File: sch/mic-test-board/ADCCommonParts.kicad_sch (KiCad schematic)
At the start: 16 parts, among them U1 LMK1C1102, U3 MAX6070BAUT41+T, X1 KC3225Z32.7680C1KX00

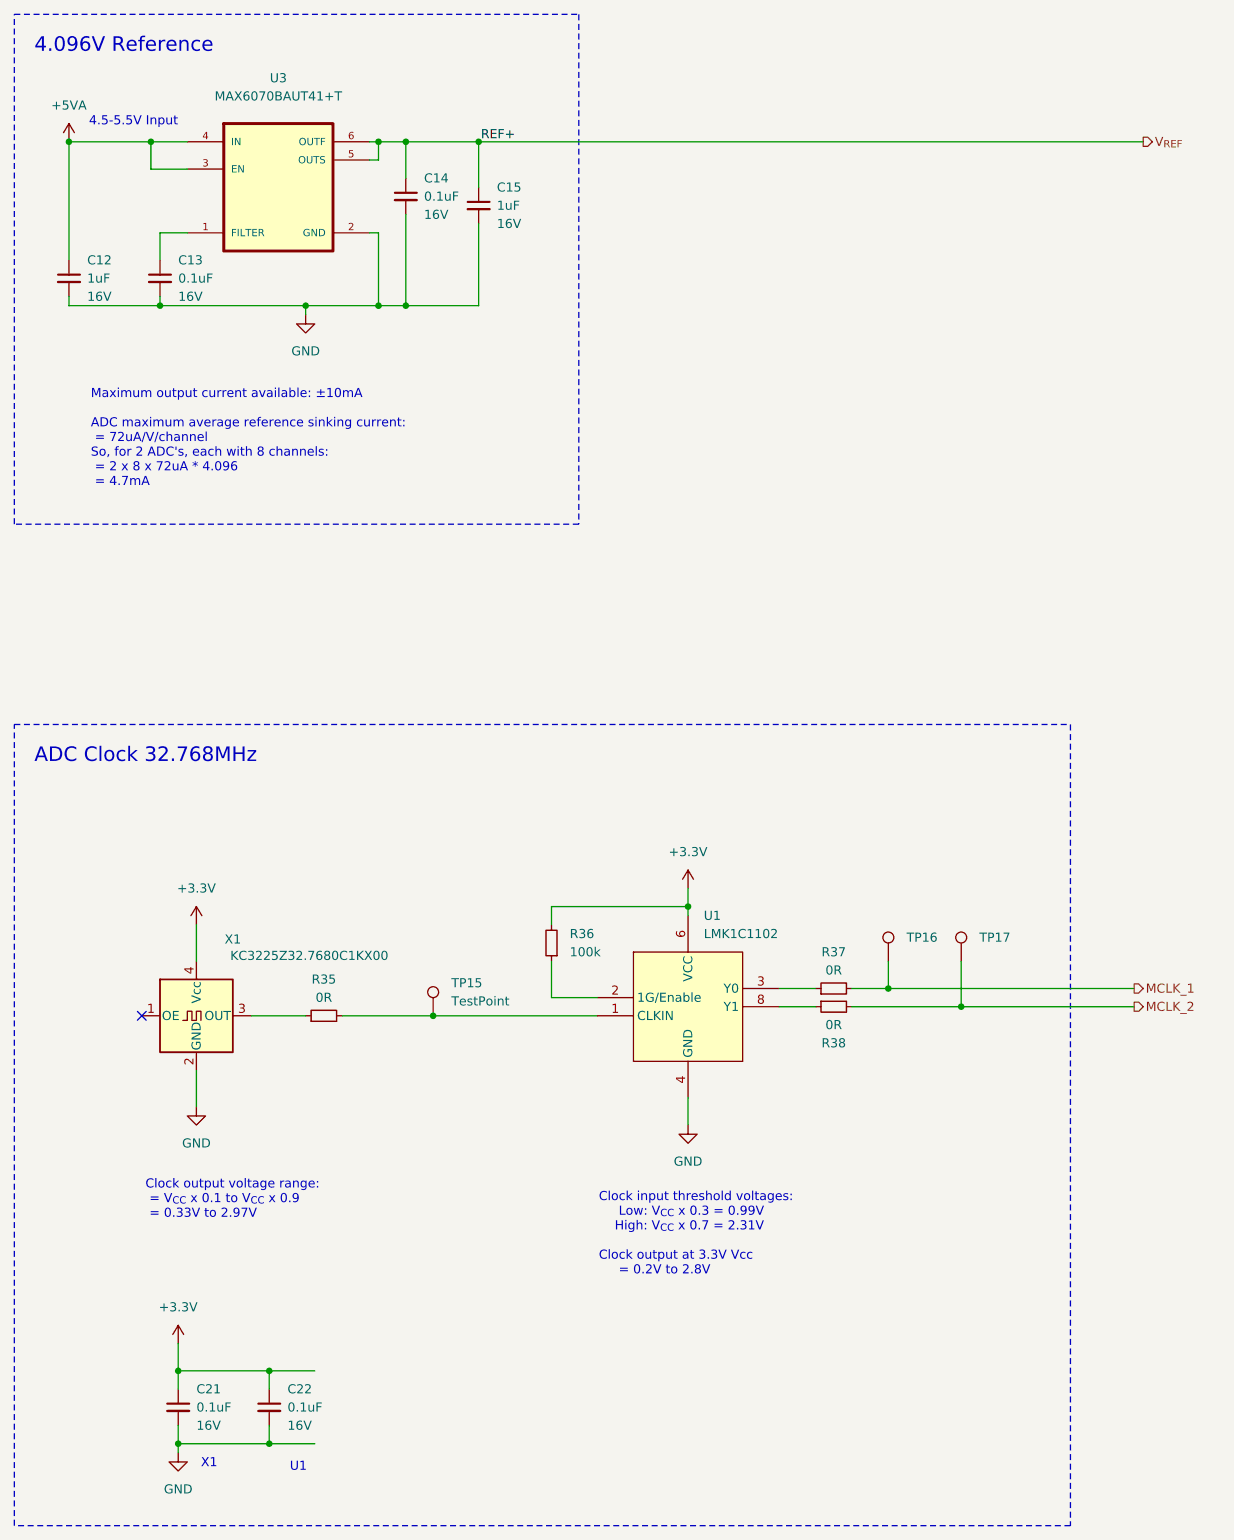
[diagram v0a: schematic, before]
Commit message: pcb: commit before large routing effort
 - schematic refactor to split preamps to each mic board
 - Mic board and main board are placed
 - no tracks laid
 - critical parts selected
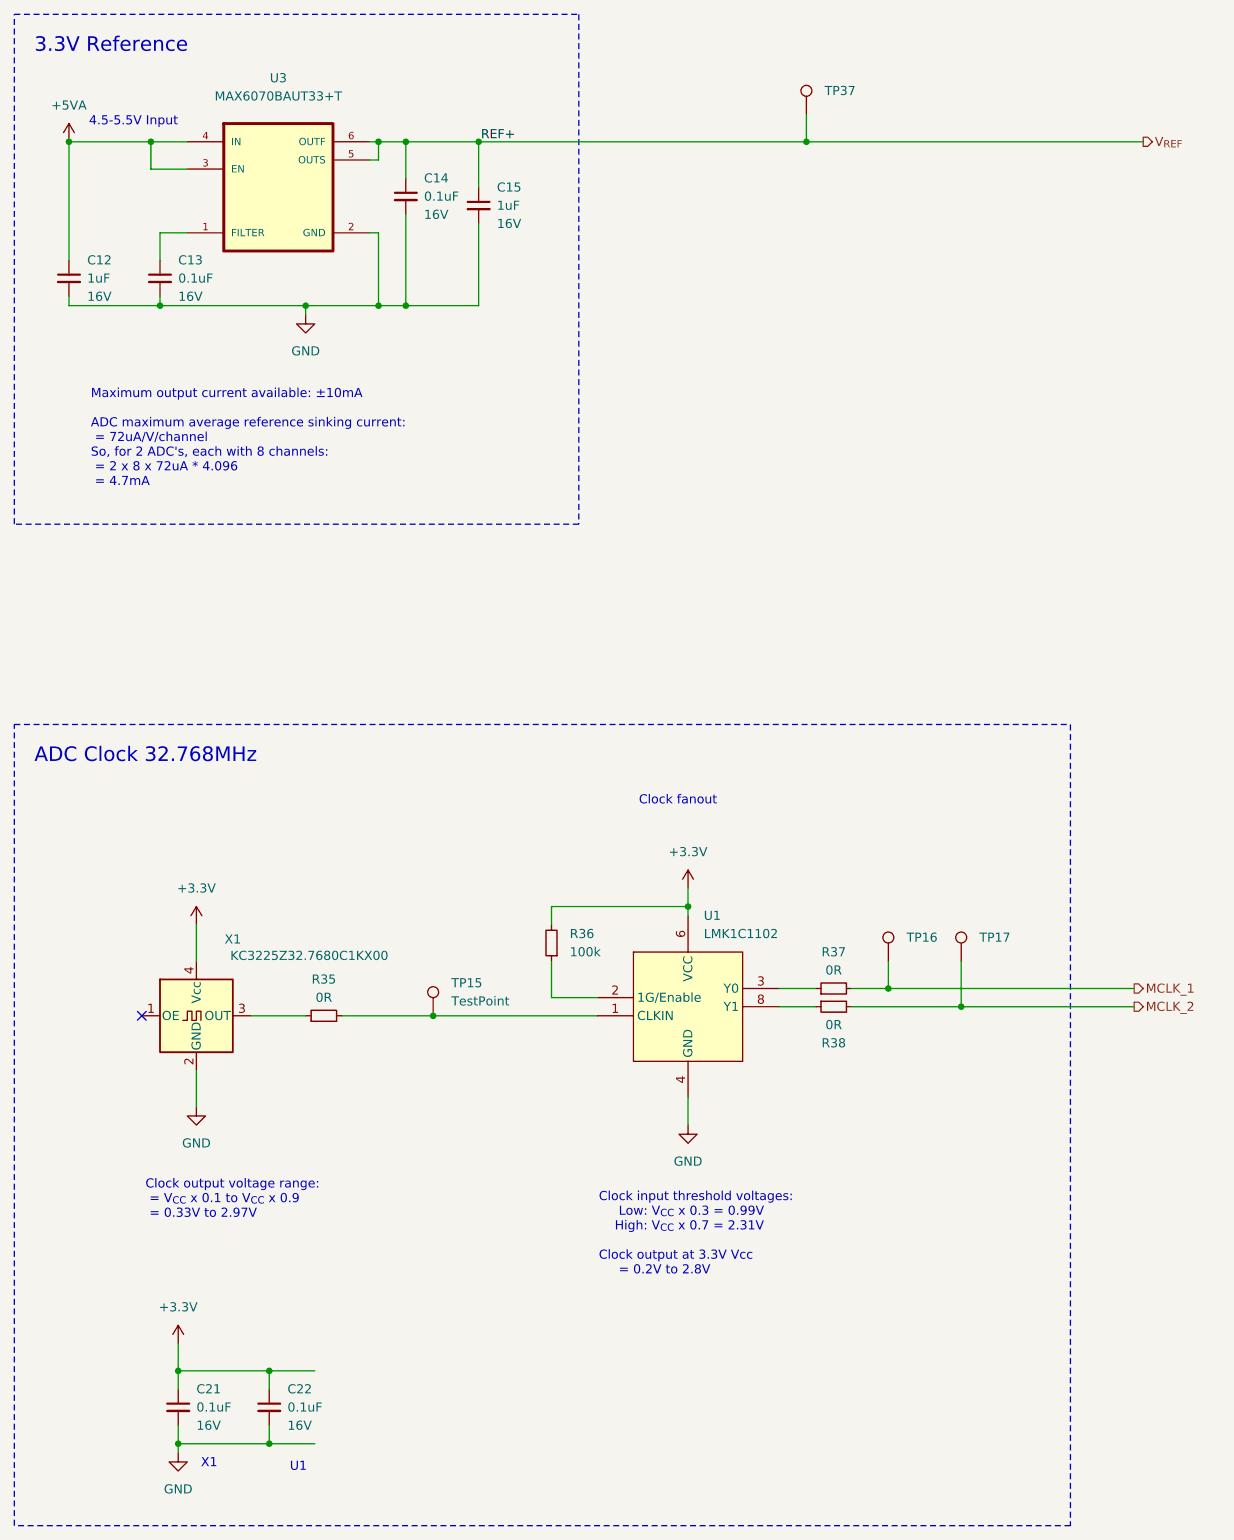
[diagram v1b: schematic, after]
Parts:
- added TP37: TestPoint, TestPoint:TestPoint_Pad_D1.0mm, symbol Connector:TestPoint
- C12, C13, C14, C15, C21, C22: footprint (none) -> Capacitor_SMD:C_0603_1608Metric
- R35, R36, R37, R38: footprint (none) -> Resistor_SMD:R_0603_1608Metric
- TP15, TP16, TP17: footprint (none) -> TestPoint:TestPoint_Pad_D1.0mm
- U3: value MAX6070BAUT41+T -> MAX6070BAUT33+T; Manufacturer (none) -> Analog Devices Inc./Maxim Integrated; Part Number MAX6070BAUT41+T -> MAX6070BAUT33+T; Supplier (none) -> Digi-Key; Supplier Number (none) -> MAX6070BAUT33+TCT-ND
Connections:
- net V_{REF}: now also TP37.1
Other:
- note added: "3.3V Reference"
- note added: "Clock fanout"
- note removed: "4.096V Reference"
- company: (none) -> Josh Berry
- title: (none) -> Sound Compass POC
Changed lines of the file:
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@@
 	(generator_version "8.0")
 	(paper "A3")
+	(title_block
+		(title "Sound Compass POC")
+		(date "2024-03-23")
+		(rev "A")
+		(company "Josh Berry")
+		(comment 1 "JBRRY")
+	)
 	(junction
 		(at 152.4 68.58)
@@
 	)
 	(junction
+		(at 255.27 68.58)
+		(diameter 0)
+		(color 0 0 0 0)
+	)
+	(junction
 		(at 163.83 68.58)
 		(diameter 0)
@@
 	(wire
 		(pts
-			(xy 209.55 68.58) (xy 302.26 68.58)
+			(xy 209.55 68.58) (xy 255.27 68.58)
 		)
 		(stroke
@@
 	(wire
 		(pts
+			(xy 255.27 68.58) (xy 302.26 68.58)
+		)
+		(stroke
+			(width 0)
+			(type default)
+		)
+	)
+	(wire
+		(pts
 			(xy 180.34 250.19) (xy 186.69 250.19)
 		)
@@
 		(pts
 			(xy 170.18 177.8) (xy 170.18 182.88)
+		)
+		(stroke
+			(width 0)
+			(type default)
+		)
+	)
+	(wire
+		(pts
+			(xy 255.27 64.77) (xy 255.27 68.58)
 		)
 		(stroke
@@
 		(fill
 			(type none)
+		)
+	)
+	(text "Clock fanout"
+		(exclude_from_sim no)
+		(at 231.902 160.528 0)
+		(effects
+			(font
+				(size 1.27 1.27)
+			)
+			(justify left)
 		)
 	)
@@
 		)
 	)
-	(text "4.096V Reference"
+	(text "3.3V Reference"
 		(exclude_from_sim no)
 		(at 147.574 56.388 0)
@@
 			)
 		)
-		(property "Footprint" ""
+		(property "Footprint" "Capacitor_SMD:C_0603_1608Metric"
 			(at 167.64 245.11 0)
 			(effects
@@
 			)
 		)
-		(property "Footprint" ""
+		(property "Footprint" "Capacitor_SMD:C_0603_1608Metric"
 			(at 199.39 76.2 0)
 			(effects
@@
 			)
 		)
-		(property "Footprint" ""
+		(property "Footprint" "TestPoint:TestPoint_Pad_D1.0mm"
 			(at 281.94 182.88 0)
 			(effects
@@
 			)
 		)
-		(property "Footprint" ""
+		(property "Footprint" "TestPoint:TestPoint_Pad_D1.0mm"
 			(at 271.78 182.88 0)
 			(effects
@@
 			)
 		)
-		(property "Footprint" ""
+		(property "Footprint" "Resistor_SMD:R_0603_1608Metric"
 			(at 219.71 180.34 0)
 			(effects
@@
 			)
 		)
-		(property "Footprint" ""
+		(property "Footprint" "Resistor_SMD:R_0603_1608Metric"
 			(at 187.96 190.5 0)
 			(effects
@@
 				(path "/51c8d8e6-56a1-4b17-b155-d2586571b4e9/488afb9d-f633-414b-baeb-731dcd40642f"
 					(reference "R35")
+					(unit 1)
+				)
+			)
+		)
+	)
+	(symbol
+		(lib_id "Connector:TestPoint")
+		(at 255.27 64.77 0)
+		(unit 1)
+		(exclude_from_sim no)
+		(in_bom yes)
+		(on_board yes)
+		(dnp no)
+		(fields_autoplaced yes)
+		(property "Reference" "TP37"
+			(at 257.81 61.4679 0)
+			(effects
+				(font
+					(size 1.27 1.27)
+				)
+				(justify left)
+			)
+		)
+		(property "Value" "TestPoint"
+			(at 257.81 62.7379 0)
+			(effects
+				(font
+					(size 1.27 1.27)
+				)
+				(justify left)
+				(hide yes)
+			)
+		)
+		(property "Footprint" "TestPoint:TestPoint_Pad_D1.0mm"
+			(at 260.35 64.77 0)
+			(effects
+				(font
+					(size 1.27 1.27)
+				)
+				(hide yes)
+			)
+		)
+		(property "Datasheet" "~"
+			(at 260.35 64.77 0)
+			(effects
+				(font
+					(size 1.27 1.27)
+				)
+				(hide yes)
+			)
+		)
+		(property "Description" "test point"
+			(at 255.27 64.77 0)
+			(effects
+				(font
+					(size 1.27 1.27)
+				)
+				(hide yes)
+			)
+		)
+		(pin "1"
+		)
+		(instances
+			(project "mic-test-pcb"
+				(path "/51c8d8e6-56a1-4b17-b155-d2586571b4e9/488afb9d-f633-414b-baeb-731dcd40642f"
+					(reference "TP37")
 					(unit 1)
 				)
@@
 			)
 		)
-		(property "Footprint" ""
+		(property "Footprint" "Capacitor_SMD:C_0603_1608Metric"
 			(at 209.55 77.47 0)
 			(effects
@@
 			)
 		)
-		(property "Footprint" ""
+		(property "Footprint" "TestPoint:TestPoint_Pad_D1.0mm"
 			(at 208.28 190.5 0)
 			(effects
@@
 			)
 		)
-		(property "Footprint" ""
+		(property "Footprint" "Resistor_SMD:R_0603_1608Metric"
 			(at 259.08 189.23 0)
 			(effects
@@
 			)
 		)
-		(property "Value" "MAX6070BAUT41+T"
+		(property "Value" "MAX6070BAUT33+T"
 			(at 181.61 62.23 0)
 			(effects
@@
 			)
 		)
-		(property "Part Number" "MAX6070BAUT41+T"
+		(property "Part Number" "MAX6070BAUT33+T"
 			(at 181.61 64.77 0)
 			(effects
@@
 			)
 		)
-		(property "Manufacturer" ""
+		(property "Manufacturer" "Analog Devices Inc./Maxim Integrated"
 			(at 181.61 76.2 0)
 			(effects
@@
 			)
 		)
-		(property "Supplier" ""
+		(property "Supplier" "Digi-Key"
 			(at 181.61 76.2 0)
 			(effects
@@
 			)
 		)
-		(property "Supplier Number" ""
+		(property "Supplier Number" "MAX6070BAUT33+TCT-ND"
 			(at 181.61 76.2 0)
 			(effects
@@
 			)
 		)
-		(property "Footprint" ""
+		(property "Footprint" "Capacitor_SMD:C_0603_1608Metric"
 			(at 165.1 87.63 0)
 			(effects
@@
 			)
 		)
-		(property "Footprint" ""
+		(property "Footprint" "Capacitor_SMD:C_0603_1608Metric"
 			(at 152.4 87.63 0)
 			(effects
@@
 			)
 		)
-		(property "Footprint" ""
+		(property "Footprint" "Capacitor_SMD:C_0603_1608Metric"
 			(at 180.34 245.11 0)
 			(effects
@@
 			)
 		)
-		(property "Footprint" ""
+		(property "Footprint" "Resistor_SMD:R_0603_1608Metric"
 			(at 259.08 186.69 0)
 			(effects

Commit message: pcb: finished routing mic board and ADC board.
 - BOM complete
 - uController pinout configured with CubeMX and re-checked
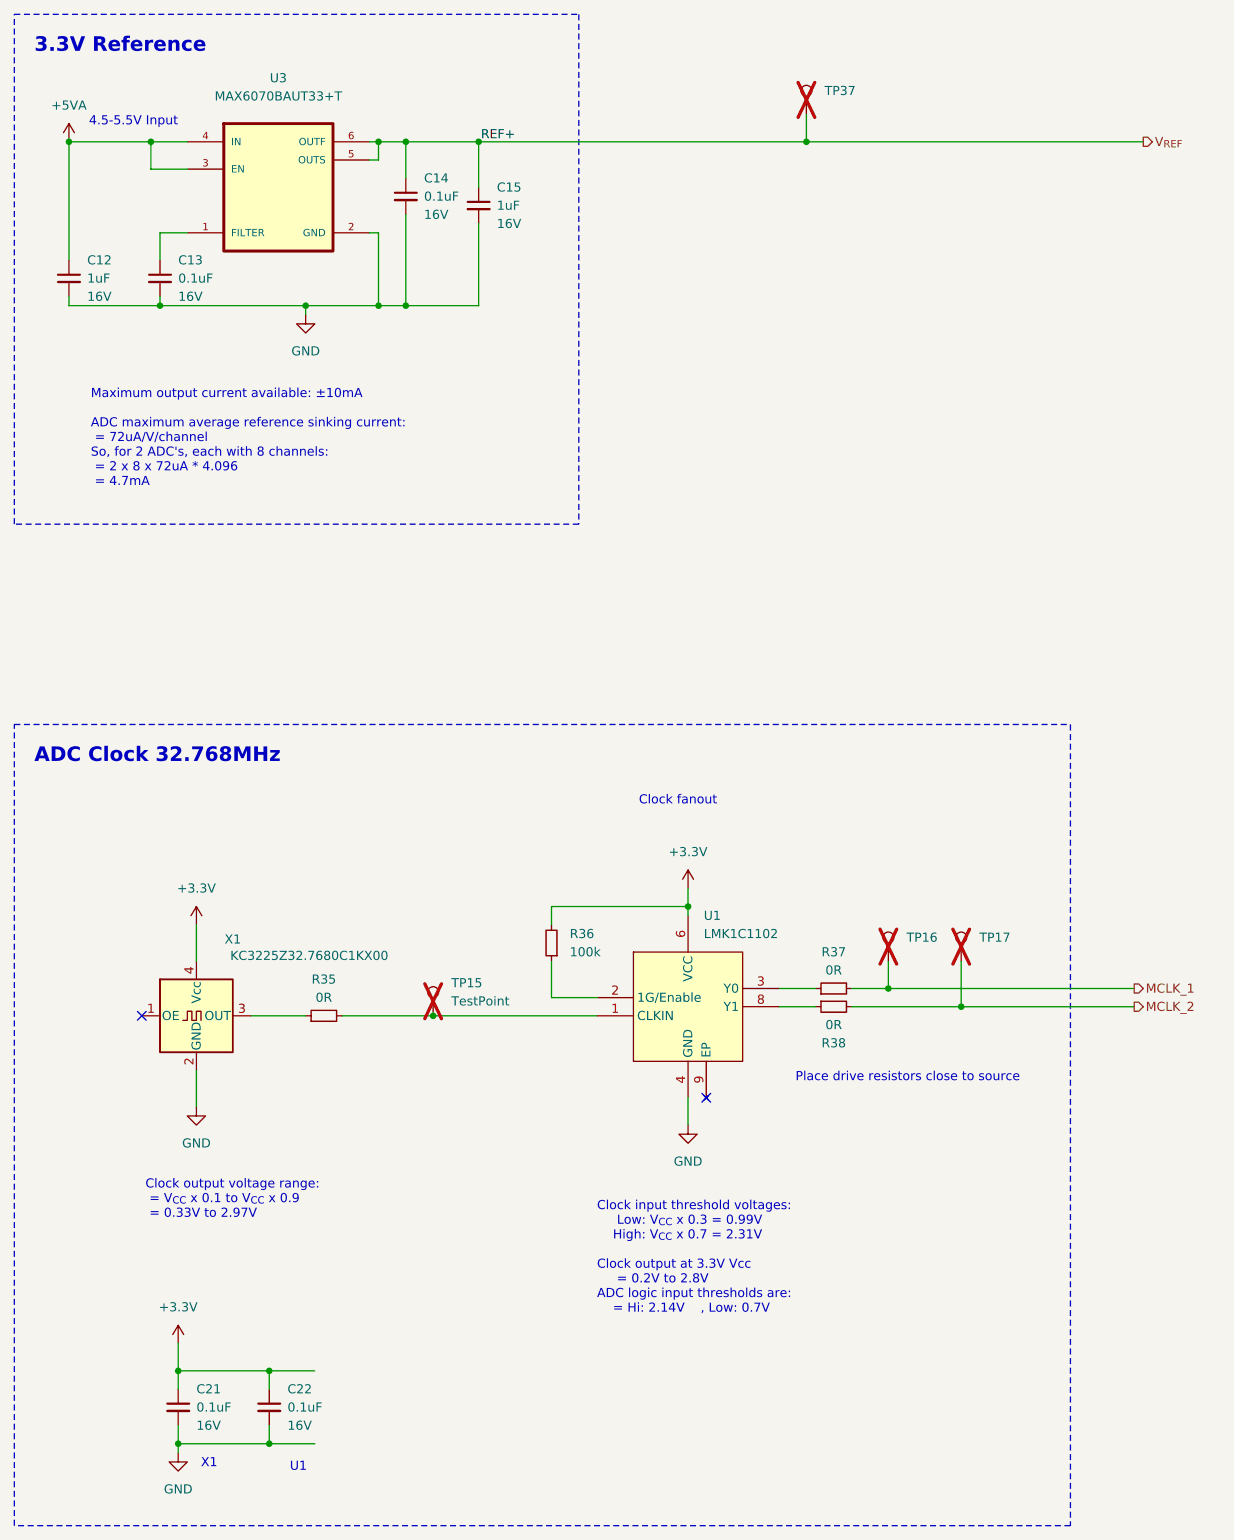
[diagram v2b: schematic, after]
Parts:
- C12, C15: Manufacturer (none) -> YAGEO; Part Number (none) -> CC0603KRX7R7BB105; Supplier (none) -> Digi-Key; Supplier Number (none) -> 311-1446-1-ND
- C13, C14, C21, C22: Manufacturer (none) -> YAGEO; Part Number (none) -> CC0603KRX7R7BB104; Supplier (none) -> Digi-Key; Supplier Number (none) -> 311-1088-1-ND
- R35, R37, R38: Manufacturer (none) -> Stackpole Electronics Inc; Part Number (none) -> RMCF0603ZT0R00; Supplier (none) -> Digi-Key; Supplier Number (none) -> RMCF0603ZT0R00CT-ND
- R36: Manufacturer (none) -> YAGEO; Part Number (none) -> RC0603FR-07100KL; Supplier (none) -> Digi-Key; Supplier Number (none) -> 311-100KHRCT-ND
- TP15, TP16, TP17, TP37: now not fitted
- U1: Manufacturer (none) -> Texas Instruments; Part Number (none) -> LMK1C1102DQFR; Supplier (none) -> Digi-Key; Supplier Number (none) -> 296-LMK1C1102DQFRCT-ND
- X1: Manufacturer (none) -> KYOCERA AVX; Part Number (none) -> KC3225Z32.7680C1KX00; Supplier (none) -> Digi-Key; Supplier Number (none) -> 478-KC3225Z32.7680C1KX00CT-ND
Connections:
- no-connect marks 1 -> 2
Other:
- note added: "Clock input threshold voltages: Low: V_{CC} x 0.3 = 0.99V High: V_{CC} x 0.7 = 2.31V Clock output at 3.3V Vcc = 0.2V to 2.8V ADC logic input thresholds are: = Hi: 2.14V , Low: 0.7V"
- note added: "Place drive resistors close to source"
- note removed: "Clock input threshold voltages: Low: V_{CC} x 0.3 = 0.99V High: V_{CC} x 0.7 = 2.31V Clock output at 3.3V Vcc = 0.2V to 2.8V"

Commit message: pcb: ordered PCB's and BOM! RevA and v240506
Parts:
- TP15, TP16, TP17, TP37: now fitted; now left out of the parts list
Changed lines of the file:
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@@
 		(unit 1)
 		(exclude_from_sim no)
-		(in_bom yes)
+		(in_bom no)
 		(on_board yes)
-		(dnp yes)
+		(dnp no)
 		(fields_autoplaced yes)
 		(property "Reference" "TP17"
@@
 		)
 		(property "Description" "test point"
+			(at 276.86 182.88 0)
+			(effects
+				(font
+					(size 1.27 1.27)
+				)
+				(hide yes)
+			)
+		)
+		(property "Manufacturer" "~"
+			(at 276.86 182.88 0)
+			(effects
+				(font
+					(size 1.27 1.27)
+				)
+				(hide yes)
+			)
+		)
+		(property "Part Number" "~"
+			(at 276.86 182.88 0)
+			(effects
+				(font
+					(size 1.27 1.27)
+				)
+				(hide yes)
+			)
+		)
+		(property "Supplier" "~"
+			(at 276.86 182.88 0)
+			(effects
+				(font
+					(size 1.27 1.27)
+				)
+				(hide yes)
+			)
+		)
+		(property "Supplier Number" "~"
 			(at 276.86 182.88 0)
 			(effects
@@
 		(unit 1)
 		(exclude_from_sim no)
-		(in_bom yes)
+		(in_bom no)
 		(on_board yes)
-		(dnp yes)
+		(dnp no)
 		(fields_autoplaced yes)
 		(property "Reference" "TP16"
@@
 		)
 		(property "Description" "test point"
+			(at 266.7 182.88 0)
+			(effects
+				(font
+					(size 1.27 1.27)
+				)
+				(hide yes)
+			)
+		)
+		(property "Manufacturer" "~"
+			(at 266.7 182.88 0)
+			(effects
+				(font
+					(size 1.27 1.27)
+				)
+				(hide yes)
+			)
+		)
+		(property "Part Number" "~"
+			(at 266.7 182.88 0)
+			(effects
+				(font
+					(size 1.27 1.27)
+				)
+				(hide yes)
+			)
+		)
+		(property "Supplier" "~"
+			(at 266.7 182.88 0)
+			(effects
+				(font
+					(size 1.27 1.27)
+				)
+				(hide yes)
+			)
+		)
+		(property "Supplier Number" "~"
 			(at 266.7 182.88 0)
 			(effects
@@
 		(unit 1)
 		(exclude_from_sim no)
-		(in_bom yes)
+		(in_bom no)
 		(on_board yes)
-		(dnp yes)
+		(dnp no)
 		(fields_autoplaced yes)
 		(property "Reference" "TP37"
@@
 		)
 		(property "Description" "test point"
+			(at 255.27 64.77 0)
+			(effects
+				(font
+					(size 1.27 1.27)
+				)
+				(hide yes)
+			)
+		)
+		(property "Manufacturer" "~"
+			(at 255.27 64.77 0)
+			(effects
+				(font
+					(size 1.27 1.27)
+				)
+				(hide yes)
+			)
+		)
+		(property "Part Number" "~"
+			(at 255.27 64.77 0)
+			(effects
+				(font
+					(size 1.27 1.27)
+				)
+				(hide yes)
+			)
+		)
+		(property "Supplier" "~"
+			(at 255.27 64.77 0)
+			(effects
+				(font
+					(size 1.27 1.27)
+				)
+				(hide yes)
+			)
+		)
+		(property "Supplier Number" "~"
 			(at 255.27 64.77 0)
 			(effects
@@
 		(unit 1)
 		(exclude_from_sim no)
-		(in_bom yes)
+		(in_bom no)
 		(on_board yes)
-		(dnp yes)
+		(dnp no)
 		(fields_autoplaced yes)
 		(property "Reference" "TP15"
@@
 			(at 203.2 190.5 0)
 			(effects
+				(font
+					(size 1.27 1.27)
+				)
+				(hide yes)
+			)
+		)
+		(property "Manufacturer" "~"
+			(at 203.2 190.5 0)
+			(effects
+				(font
+					(size 1.27 1.27)
+				)
+				(hide yes)
+			)
+		)
+		(property "Part Number" "~"
+			(at 203.2 190.5 0)
+			(effects
+				(font
+					(size 1.27 1.27)
+				)
+				(hide yes)
+			)
+		)
+		(property "Supplier" "~"
+			(at 203.2 190.5 0)
+			(effects
+				(font
+					(size 1.27 1.27)
+				)
+				(hide yes)
+			)
+		)
+		(property "Supplier Number" "~"
+			(at 203.2 190.5 0)
+			(effects

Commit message: sch: adding bringup notes
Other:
- note added: "24.576MHz drop in: 478-KC3225Z24.5760C1KX00CT-ND"
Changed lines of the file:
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@@
+		)
+	)
+	(text "24.576MHz drop in:\n478-KC3225Z24.5760C1KX00CT-ND"
+		(exclude_from_sim no)
+		(at 171.958 164.084 0)
+		(effects
+			(font
+				(size 1.27 1.27)
+			)
 		)
 	)
